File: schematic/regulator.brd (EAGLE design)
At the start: 62 x 43 mm, 24 parts, among them J1 COMM, J2 STOP_LIGHT, J3 ON/OFF, J4 IN, J5 DRIVER, Q1 NMOSFETSOT23, Q2 NMOSFETSOT23, Q3 NMOSFETSOT23, U1 MAX5035DIP8

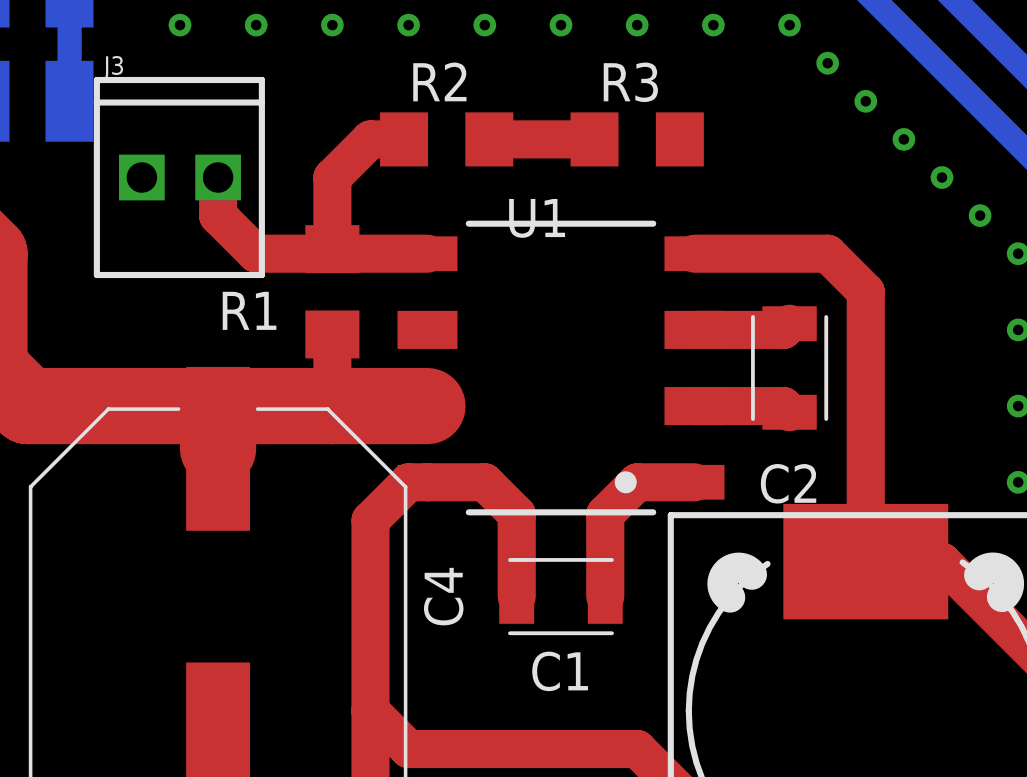
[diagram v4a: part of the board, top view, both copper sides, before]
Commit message: Change MAX regulator package
- Change MAX package to drill-pin
- Move button to bottom layout
- Move elements for better work on regulator and ECU
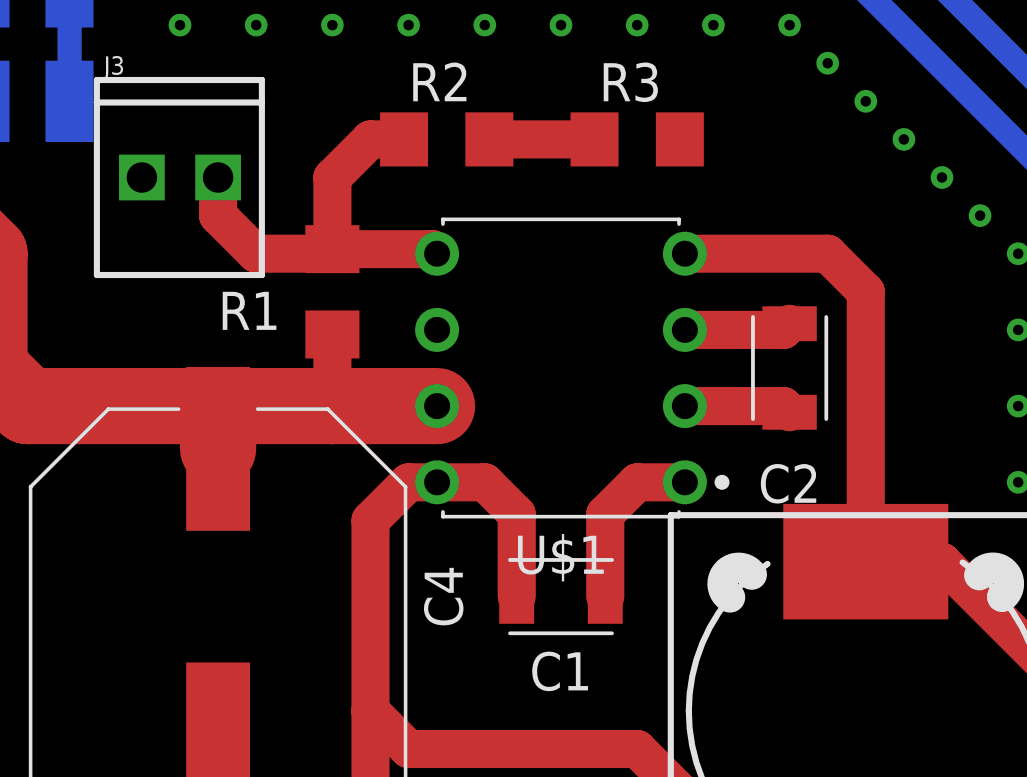
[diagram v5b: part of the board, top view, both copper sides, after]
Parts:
- removed U1: MAX5035DIP8, regulator:DIP8
- added U$1: MAX5035PDIP8, eScooter:DIP826W56P254L937H458Q8B
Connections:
- net 12V: now also U$1.4; no longer U1.4
- net GND: now also U$1.3, U$1.6; no longer U1.3, U1.6
- net N$1: now also U$1.1; no longer U1.1
- net N$2: now also U$1.8; no longer U1.8
- net N$4: now also U$1.2; no longer U1.2
- net N$5: now also U$1.5; no longer U1.5
- net VIN: now also U$1.7; no longer U1.7
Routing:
- net N$5: track 14.3 -> 14.8 mm
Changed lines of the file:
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@@
 <attribute name="VALUE" x="33.02" y="34.29" size="1.27" layer="27" rot="R180"/>
-</element>
-<element name="U1" library="regulator" package="DIP8" package3d_urn="urn:adsk.eagle:package:8089856/1" value="MAX5035DIP8" x="29.21" y="24.13" smashed="yes" rot="R90">
-<attribute name="NAME" x="27.3449" y="28.495" size="1.27" layer="25"/>
-<attribute name="VALUE" x="33.6151" y="31.035" size="1.27" layer="27" rot="R180"/>
 </element>
 <element name="J3" library="SparkFun-Connectors" library_urn="urn:adsk.eagle:library:513" package="1X02_2.54_SCREWTERM" package3d_urn="urn:adsk.eagle:package:38059/1" value="ON/OFF" x="15.24" y="30.48" smashed="yes">
@@
 <attribute name="VALUE" x="10.895" y="16.51" size="1.27" layer="27" rot="R270" align="top-center"/>
 </element>
+<element name="U$1" library="eScooter" package="DIP826W56P254L937H458Q8B" package3d_urn="urn:adsk.eagle:package:22059831/1" value="MAX5035PDIP8" x="29.21" y="24.13" smashed="yes" rot="R180">
+<attribute name="NAME" x="29.21" y="18.54" size="1.27" layer="25" rot="R180" align="bottom-center"/>
+<attribute name="VALUE" x="29.21" y="29.72" size="1.27" layer="27" rot="R180" align="top-center"/>
+</element>
 </elements>
 <signals>
 <signal name="GND">
-<contactref element="U1" pad="6"/>
-<contactref element="U1" pad="3"/>
 <contactref element="C2" pad="1"/>
 <contactref element="D1" pad="A"/>
@@
 <contactref element="J4" pad="1"/>
 <contactref element="J3" pad="P2"/>
-<wire x1="36.83" y1="25.6054" x2="36.6246" y2="25.4" width="1.27" layer="1"/>
-<wire x1="36.6246" y1="25.4" x2="33.66" y2="25.4" width="1.27" layer="1"/>
 <polygon width="1.27" layer="1">
 <vertex x="0" y="43"/>
@@
 <contactref element="R8" pad="2"/>
 <contactref element="C4" pad="2"/>
+<contactref element="U$1" pad="6"/>
+<contactref element="U$1" pad="3"/>
+<wire x1="33.34" y1="25.4" x2="36.6246" y2="25.4" width="1.27" layer="1"/>
+<wire x1="36.6246" y1="25.4" x2="36.83" y2="25.6054" width="1.27" layer="1"/>
 </signal>
 <signal name="VIN">
-<contactref element="U1" pad="7"/>
 <contactref element="R1" pad="1"/>
 <contactref element="J4" pad="2"/>
-<wire x1="24.76" y1="22.86" x2="21.59" y2="22.86" width="2.54" layer="1"/>
 <wire x1="21.59" y1="25.248" x2="21.59" y2="22.86" width="1.27" layer="1"/>
 <wire x1="2.54" y1="31.19" x2="6.91" y2="31.19" width="2.54" layer="1"/>
@@
 <wire x1="11.43" y1="22.86" x2="10.16" y2="24.13" width="2.54" layer="1"/>
 <wire x1="10.16" y1="27.94" x2="10.16" y2="24.13" width="2.54" layer="1"/>
-<wire x1="21.59" y1="22.86" x2="17.78" y2="22.86" width="2.54" layer="1"/>
+<wire x1="17.78" y1="22.86" x2="21.59" y2="22.86" width="2.54" layer="1"/>
 <wire x1="17.78" y1="22.86" x2="11.43" y2="22.86" width="2.54" layer="1"/>
 <wire x1="17.78" y1="21.435" x2="17.78" y2="22.86" width="2.54" layer="1"/>
+<contactref element="U$1" pad="7"/>
+<wire x1="21.59" y1="22.86" x2="25.08" y2="22.86" width="2.54" layer="1"/>
 </signal>
 <signal name="N$1">
-<contactref element="U1" pad="1"/>
 <contactref element="C1" pad="1"/>
 <wire x1="30.6854" y1="16.51" x2="30.6854" y2="19.2554" width="1.27" layer="1"/>
-<wire x1="30.6854" y1="19.2554" x2="31.75" y2="20.32" width="1.27" layer="1"/>
-<wire x1="31.75" y1="20.32" x2="33.66" y2="20.32" width="1.27" layer="1"/>
+<wire x1="31.75" y1="20.32" x2="30.6854" y2="19.2554" width="1.27" layer="1"/>
+<contactref element="U$1" pad="1"/>
+<wire x1="33.34" y1="20.32" x2="31.75" y2="20.32" width="1.27" layer="1"/>
 </signal>
 <signal name="N$2">
 <contactref element="C1" pad="2"/>
-<contactref element="U1" pad="8"/>
 <contactref element="D1" pad="C"/>
 <contactref element="L1" pad="1"/>
 <wire x1="27.7346" y1="16.51" x2="27.7346" y2="19.2554" width="1.27" layer="1"/>
-<wire x1="27.7346" y1="19.2554" x2="26.67" y2="20.32" width="1.27" layer="1"/>
-<wire x1="26.67" y1="20.32" x2="24.76" y2="20.32" width="1.27" layer="1"/>
-<wire x1="24.76" y1="20.32" x2="24.13" y2="20.32" width="1.27" layer="1"/>
-<wire x1="24.13" y1="20.32" x2="22.86" y2="19.05" width="1.27" layer="1"/>
+<wire x1="26.67" y1="20.32" x2="27.7346" y2="19.2554" width="1.27" layer="1"/>
+<wire x1="22.86" y1="19.05" x2="24.13" y2="20.32" width="1.27" layer="1"/>
 <wire x1="22.86" y1="12.7" x2="22.86" y2="19.05" width="1.27" layer="1"/>
 <wire x1="29.06" y1="5.08" x2="25.4" y2="5.08" width="1.27" layer="1"/>
@@
 <wire x1="39.37" y1="7.725" x2="35.455" y2="7.725" width="1.27" layer="1"/>
 <wire x1="35.455" y1="7.725" x2="31.75" y2="11.43" width="1.27" layer="1"/>
+<contactref element="U$1" pad="8"/>
+<wire x1="24.13" y1="20.32" x2="25.08" y2="20.32" width="1.27" layer="1"/>
+<wire x1="25.08" y1="20.32" x2="26.67" y2="20.32" width="1.27" layer="1"/>
 </signal>
 <signal name="12V">
 <contactref element="L1" pad="2"/>
-<contactref element="U1" pad="4"/>
 <contactref element="C3" pad="1"/>
 <wire x1="39.37" y1="26.67" x2="38.1" y2="27.94" width="1.27" layer="1"/>
-<wire x1="33.66" y1="27.94" x2="38.1" y2="27.94" width="1.27" layer="1"/>
 <wire x1="39.37" y1="26.67" x2="39.37" y2="17.675" width="1.27" layer="1"/>
 <contactref element="J1" pad="1"/>
@@
 <contactref element="D2" pad="1"/>
 <wire x1="53.34" y1="8.45" x2="53.34" y2="6.35" width="1.27" layer="1"/>
+<contactref element="U$1" pad="4"/>
+<wire x1="38.1" y1="27.94" x2="33.34" y2="27.94" width="1.27" layer="1"/>
 </signal>
 <signal name="N$4">
 <contactref element="C2" pad="2"/>
-<contactref element="U1" pad="2"/>
 <wire x1="36.6246" y1="22.86" x2="36.83" y2="22.6546" width="1.27" layer="1"/>
-<wire x1="33.66" y1="22.86" x2="36.6246" y2="22.86" width="1.27" layer="1"/>
+<contactref element="U$1" pad="2"/>
+<wire x1="33.34" y1="22.86" x2="36.6246" y2="22.86" width="1.27" layer="1"/>
 </signal>
 <signal name="N$5">
-<contactref element="U1" pad="5"/>
 <contactref element="R1" pad="2"/>
 <contactref element="R2" pad="1"/>
 <contactref element="J3" pad="P1"/>
 <wire x1="21.59" y1="28.092" x2="21.742" y2="27.94" width="1.27" layer="1"/>
-<wire x1="21.742" y1="27.94" x2="24.76" y2="27.94" width="1.27" layer="1"/>
 <wire x1="21.59" y1="28.092" x2="21.59" y2="30.48" width="1.27" layer="1"/>
 <wire x1="21.59" y1="30.48" x2="22.86" y2="31.75" width="1.27" layer="1"/>
@@
 <wire x1="17.78" y1="29.21" x2="19.05" y2="27.94" width="1.27" layer="1"/>
 <wire x1="19.05" y1="27.94" x2="21.742" y2="27.94" width="1.27" layer="1"/>
+<contactref element="U$1" pad="5"/>
+<wire x1="21.59" y1="28.092" x2="24.928" y2="28.092" width="1.27" layer="1"/>
+<wire x1="24.928" y1="28.092" x2="25.08" y2="27.94" width="1.27" layer="1"/>
 </signal>
 <signal name="N$7">

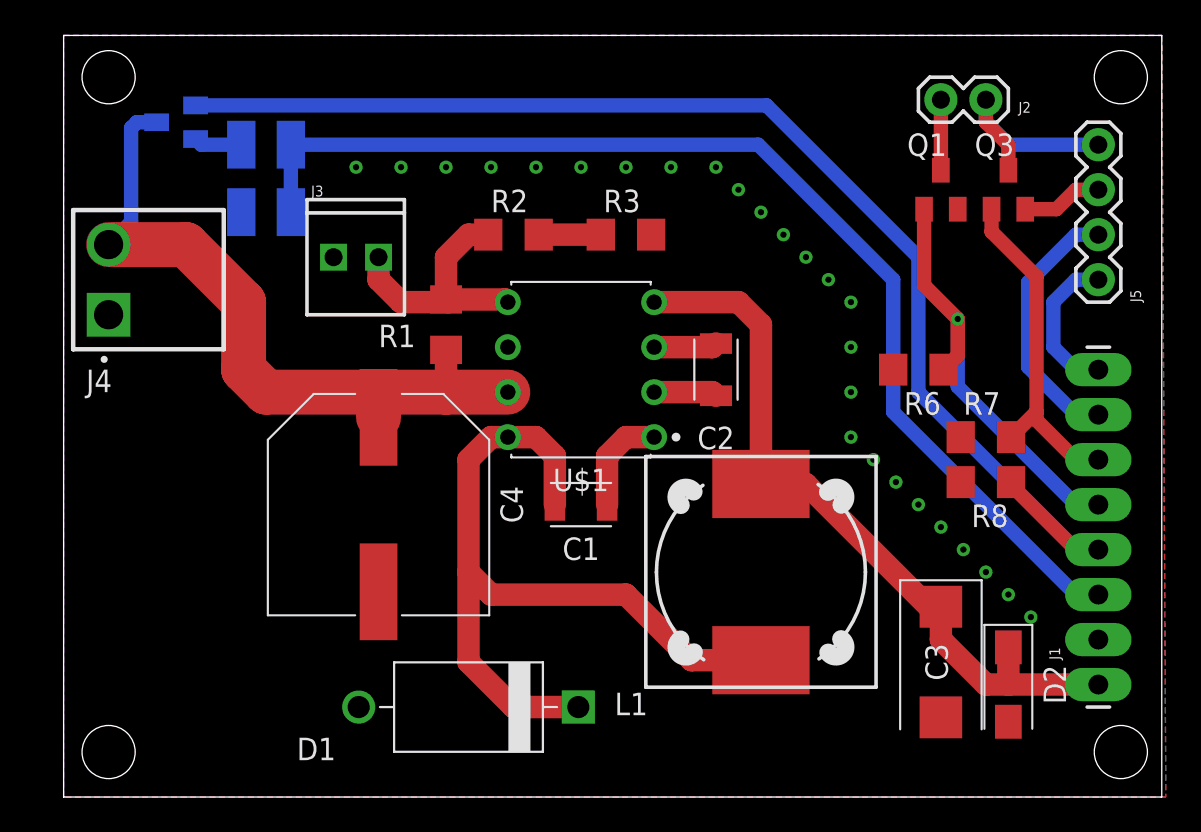
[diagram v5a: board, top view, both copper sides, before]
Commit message: Rearrange elements in regulator schematics
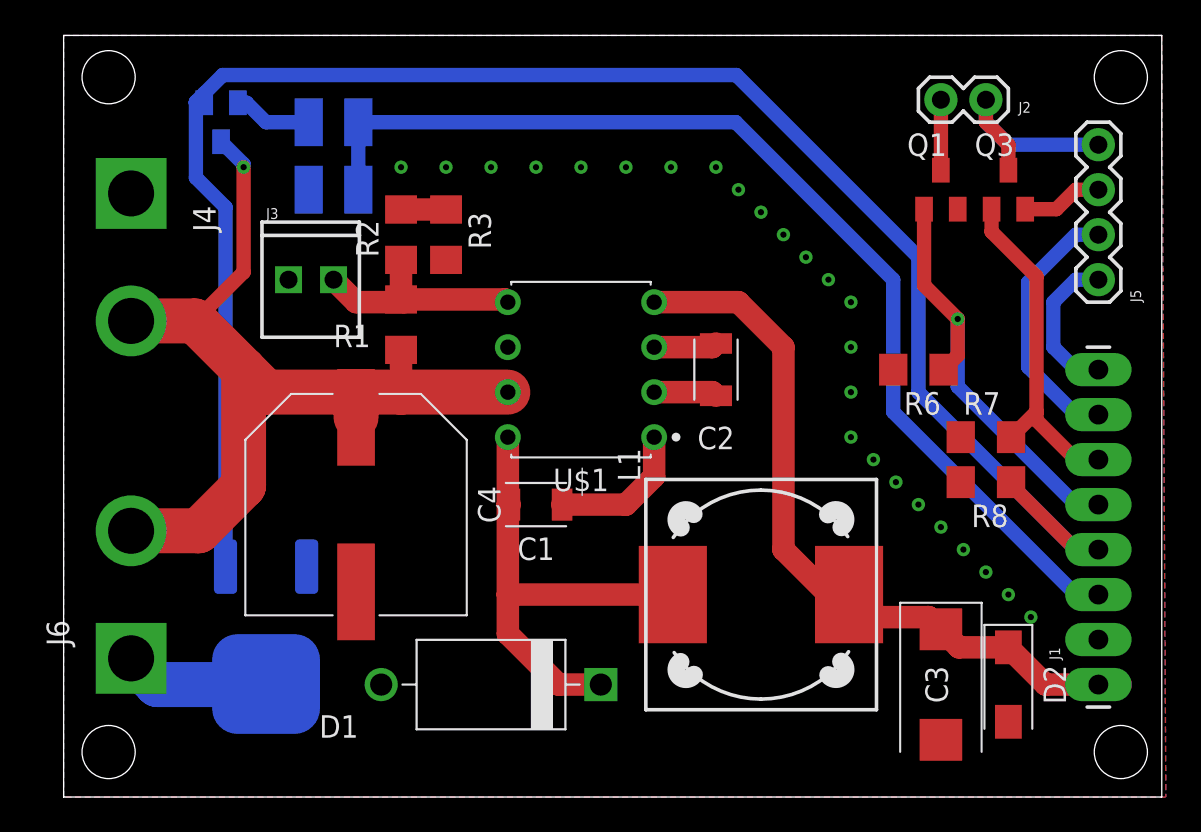
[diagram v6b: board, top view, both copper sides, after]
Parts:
- added J6: DRIVER POWER, eScooter:XT60
- added Q4: IRFR3607PBF, Transistor:DPAK3
- J4: value IN -> BATTERY; device Connectors:HDR-02 -> eScooter:XT60
- moved R3 10.2 mm to (21.6, 31.8), turned to 90 degrees
- moved R2 6.35 mm to (19.1, 31.8), turned to 90 degrees
- moved R4 4.02 mm to (15.2, 38.1)
- moved R5 4.02 mm to (15.2, 34.3)
- moved J3 2.84 mm to (12.7, 29.2)
- moved Q2 2.54 mm to (8.89, 38.1), turned to 180 degrees
- moved C1 2.54 mm to (26.7, 16.5)
- moved R1 2.54 mm to (19.1, 26.7)
- moved J4 1.80 mm to (3.81, 30.5), turned to 270 degrees
- moved D1 1.80 mm to (24.1, 6.35)
- moved C3 1.27 mm to (49.5, 6.35)
- moved C4 1.27 mm to (16.5, 16.5)
- moved L1 1.27 mm to (39.4, 11.4), turned to 0 degrees
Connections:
- new net P$1: J6.GND, Q4.3
- net GND: now also J4.GND, Q4.2; no longer J4.1
- net PWM: now also Q4.1
- net VIN: now also J4.VCC, J6.VCC; no longer J4.2
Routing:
- net PWM: track 72.4 -> 101.7 mm
- net N$2: track 45.8 -> 27.0 mm
- net VIN: track 40.7 -> 52.5 mm, vias 0 -> 1
- net P$1: track 0.00 -> 9.50 mm
- net BAT: track 64.3 -> 61.0 mm
- net N$1: track 5.84 -> 8.07 mm
- net N$8: track 2.71 -> 4.82 mm
- net N$5: track 14.8 -> 13.0 mm
- net N$7: track 3.51 -> 2.54 mm
- net GND: vias 26 -> 25

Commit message: Rework regulator PCB
- Re-arrange elements
- Add few ground drills
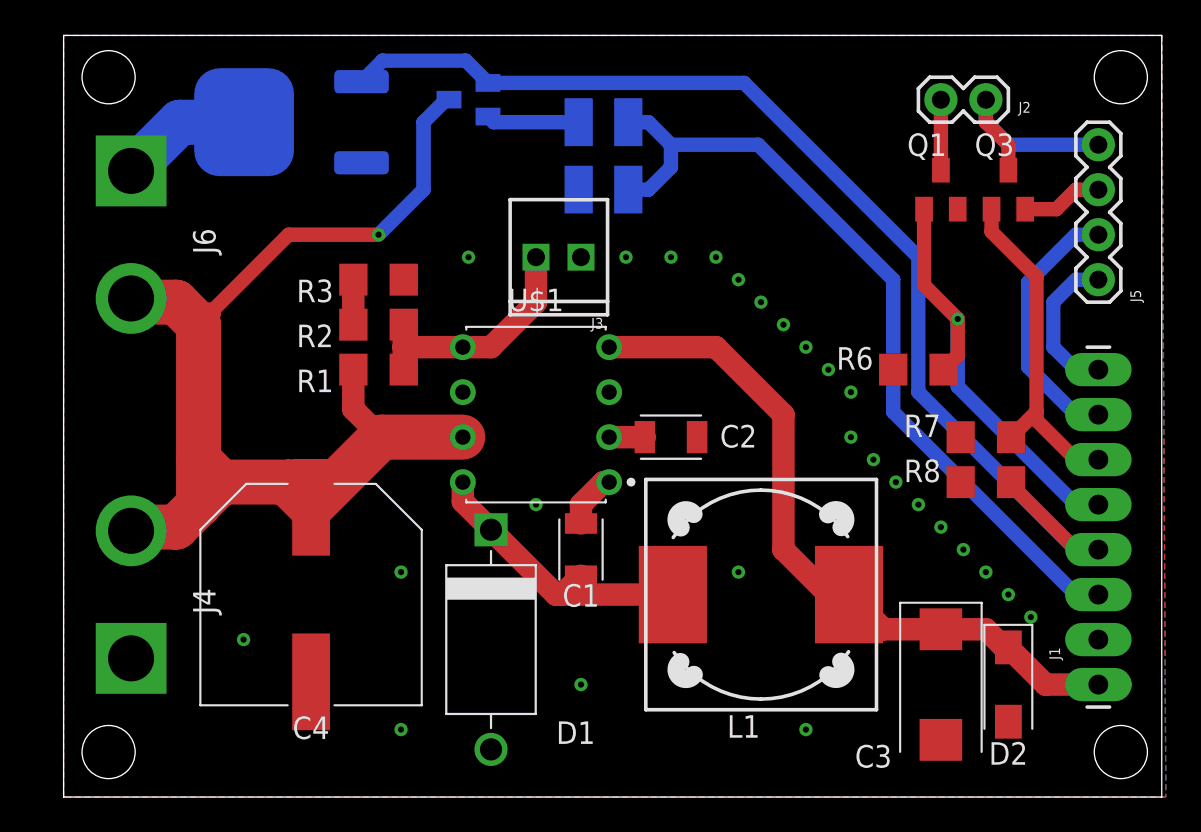
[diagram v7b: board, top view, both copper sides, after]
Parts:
- moved Q4 29.2 mm to (12.7, 38.1), turned to 270 degrees
- moved J6 20.3 mm to (3.81, 31.8), turned to 270 degrees
- moved J4 19.1 mm to (3.81, 11.4), turned to 90 degrees
- moved J3 16.6 mm to (29.2, 30.5), turned to 180 degrees
- moved R4 15.2 mm to (30.5, 38.1)
- moved R5 15.2 mm to (30.5, 34.3)
- moved Q2 14.0 mm to (22.9, 39.4), turned to 270 degrees
- moved C4 5.68 mm to (14.0, 11.4)
- moved R2 5.24 mm to (17.8, 26.7), turned to 180 degrees
- moved C2 4.58 mm to (34.3, 20.3), turned to 180 degrees
- moved R3 4.58 mm to (17.8, 29.2), turned to 180 degrees
- moved C1 3.59 mm to (29.2, 14.0), turned to 270 degrees
- moved U$1 3.59 mm to (26.7, 21.6)
- moved R1 2.84 mm to (17.8, 24.1), turned to 0 degrees
- moved D1 2.54 mm to (24.1, 8.89), turned to 270 degrees
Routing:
- net PWM: track 101.7 -> 64.6 mm
- net BAT: track 61.0 -> 46.2 mm
- net VIN: track 52.5 -> 65.9 mm
- net N$2: track 27.0 -> 16.6 mm
- net N$1: track 8.07 -> 3.18 mm
- net GND: track 3.58 -> 0.00 mm, vias 25 -> 26
- net N$4: track 3.58 -> 2.01 mm
- net P$1: track 9.50 -> 8.76 mm
- net 12V: track 42.0 -> 41.2 mm
- net N$5: track 13.0 -> 13.6 mm
